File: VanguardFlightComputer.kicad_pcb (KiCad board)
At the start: 4 copper layers, 56 x 32 mm, 62 parts, among them IC1 ST1L05CPU33R, IC2 ASM330LHHTR, IC3 MAX-M10S-00B, J1 USB_C_Receptacle, J2 MEM2067-02-180-00-A, J3 Conn_Coaxial, J4 Conn_Coaxial, U1 STM32H743VGTx, U2 LD1117S50TR_SOT223, U3 USBLC6-2P6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

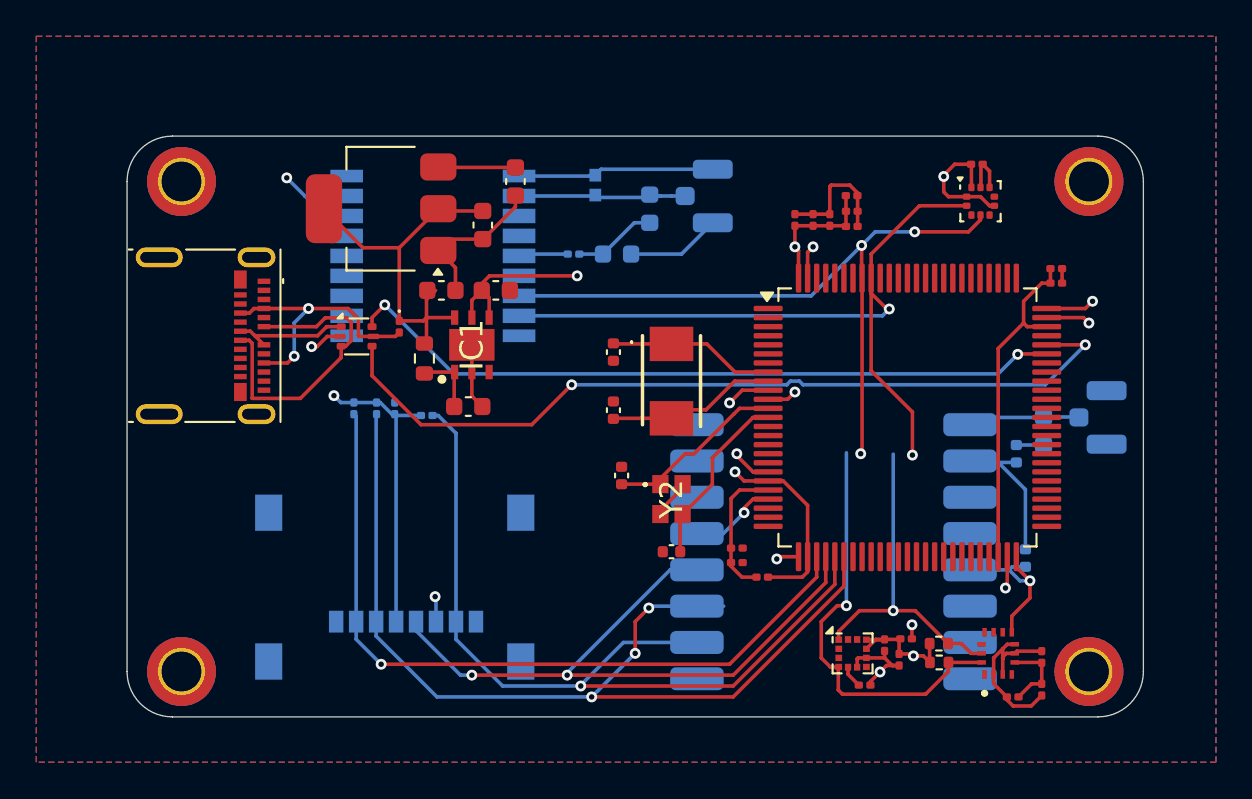
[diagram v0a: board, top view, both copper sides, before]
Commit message: Added IO
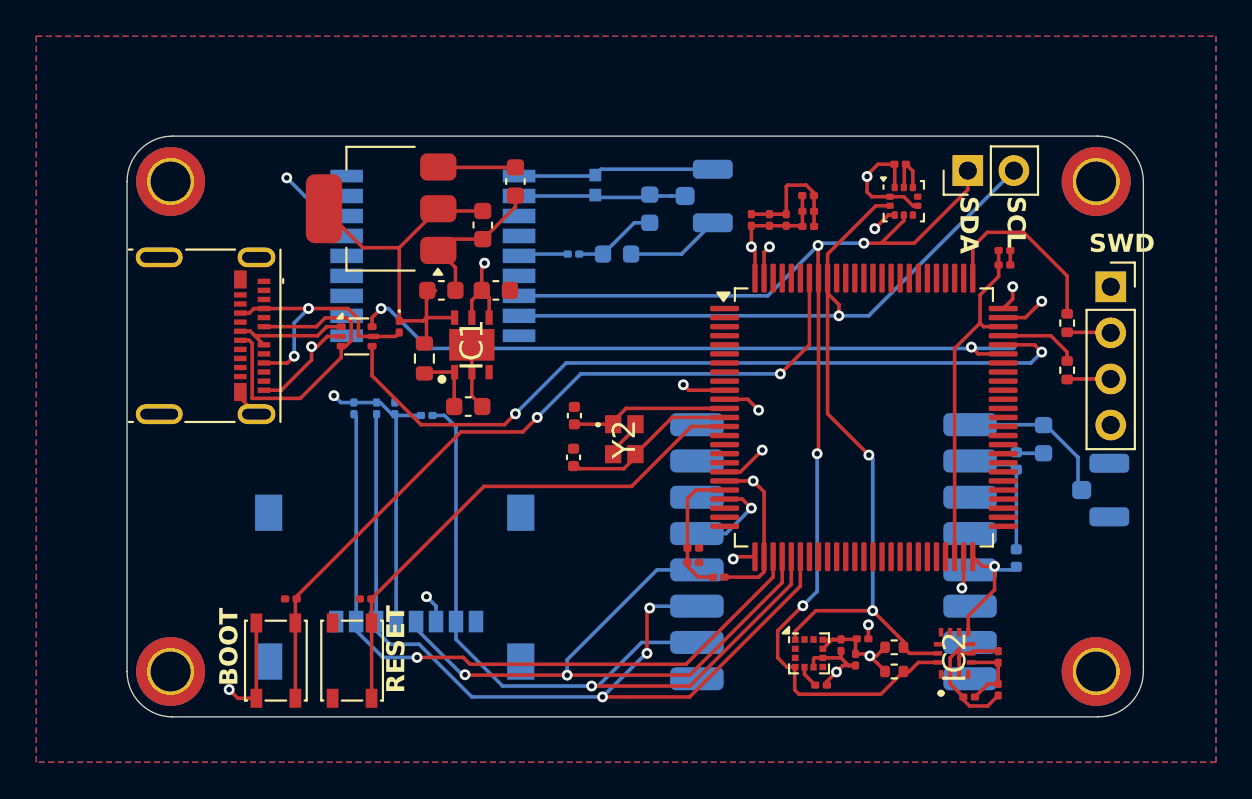
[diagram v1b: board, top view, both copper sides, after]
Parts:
- removed C16, C17: 10pF, Capacitor_SMD:C_0402_1005Metric
- removed Y1: 32.768MHz, VanguardLib:ABM3
- added C30: 100nF, Capacitor_SMD:C_0201_0603Metric, F.Cu at (103.1, 101.0)
- added J5: Conn_01x04_Pin, Connector_PinSocket_2.54mm:PinSocket_1x04_P2.54mm_Vertical, F.Cu at (144.2, 83.8)
- added J6: Conn_01x02_Pin, Connector_PinHeader_2.54mm:PinHeader_1x02_P2.54mm_Vertical, F.Cu at (136.3, 77.4)
- added R10: 100, Resistor_SMD:R_0402_1005Metric, F.Cu at (141.8, 85.8)
- added R8: 10k, Resistor_SMD:R_0201_0603Metric, F.Cu at (99.0, 101.0)
- added R9: 100, Resistor_SMD:R_0402_1005Metric, F.Cu at (141.8, 88.4)
- added SW1: SW_Push, Button_Switch_SMD:SW_SPST_PTS810, F.Cu at (102.4, 104.4)
- added SW2: SW_Push, Button_Switch_SMD:SW_SPST_PTS810, F.Cu at (98.2, 104.4)
- moved C19 7.50 mm to (114.6, 93.2), turned to -90 degrees
- moved C27 4.22 mm to (132.6, 77.0)
- moved U5 4.22 mm to (132.8, 79.1)
- moved C18 4.20 mm to (114.7, 90.9)
- moved Y2 4.20 mm to (117.4, 92.2)
- moved J4 4.00 mm to (143.7, 95.0)
- moved C14 3.03 mm to (138.3, 81.8)
- moved C15 3.03 mm to (138.3, 82.6)
- moved R3 2.90 mm to (132.3, 105.0)
- moved R2 2.61 mm to (132.3, 103.7)
- moved C5 2.40 mm to (126.3, 80.1)
- moved C20 2.40 mm to (138.0, 104.2)
- moved C21 2.40 mm to (138.0, 106.0)
- moved C22 2.40 mm to (136.4, 106.4)
- moved C24 2.40 mm to (130.5, 103.2)
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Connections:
- R2 pad 2: I2C1_SDA -> I2C1_SCL
- R3 pad 2: I2C1_SCL -> I2C1_SDA
- U1 pad 14: unconnected-(U1-NRST-Pad14) -> RST
- U1 pad 94: unconnected-(U1-BOOT0-Pad94) -> BOOT0
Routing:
- net BOOT0: track 0.00 -> 43.3 mm, vias 0 -> 2
- net RST: track 0.00 -> 28.9 mm
- net SWCLK: track 0.00 -> 10.3 mm
- net OSC32_OUT: track 9.59 -> 0.00 mm
- net OSC32_IN: track 9.38 -> 0.00 mm
- net I2C1_SCL: track 59.5 -> 68.1 mm
- net GND: track 82.1 -> 87.8 mm, vias 10 -> 11
- net SWDIO: track 0.00 -> 4.39 mm
- net SPI1_MOSI: track 53.9 -> 49.7 mm
- net SPI1_MISO: track 46.3 -> 43.4 mm
- net SD_CS: track 41.5 -> 38.8 mm
- net USB_DP: track 46.2 -> 43.6 mm
- net I2C1_SDA: track 62.6 -> 65.1 mm
- net Net-(J5-Pin_3): track 0.00 -> 2.41 mm
- net Net-(J5-Pin_2): track 0.00 -> 2.41 mm
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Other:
- board text added: "BOOT"
- board text added: "RESET"
- board text added: "SCL"
- board text added: "SDA"
- board text added: "SWD"

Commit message: Change 0201 to 0403
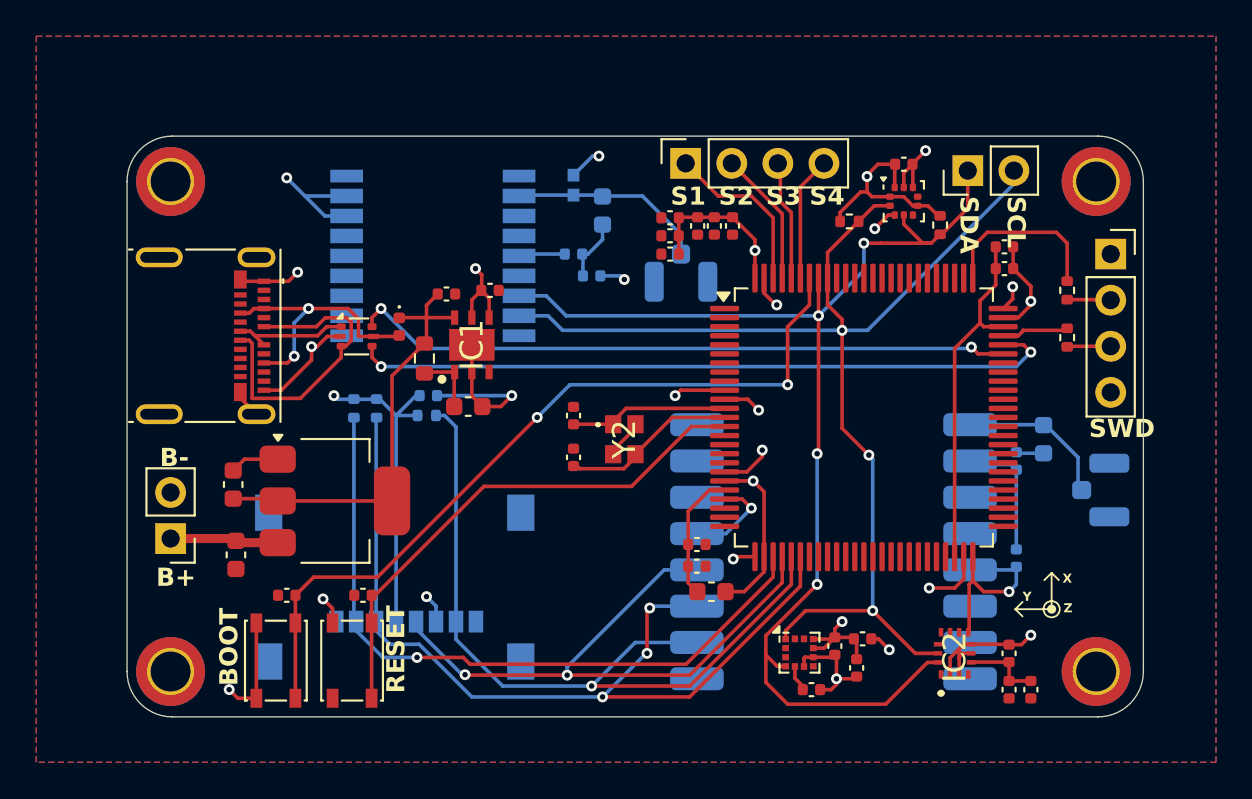
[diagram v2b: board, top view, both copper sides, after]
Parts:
- added J7: Conn_01x04_Pin, Connector_PinSocket_2.54mm:PinSocket_1x04_P2.54mm_Vertical, F.Cu at (120.8, 77.0)
- added J8: Conn_01x02_Pin, Connector_PinHeader_2.54mm:PinHeader_1x02_P2.54mm_Vertical, F.Cu at (92.4, 97.7)
- C1, C14, C15, C2, C20, C21, C22, C23, C24, C25, C26, C27, C28, C3, C30, C4, C5, C6, C7, C8: footprint Capacitor_SMD:C_0201_0603Metric -> Capacitor_SMD:C_0402_1005Metric
- C11, C12, C29: footprint Capacitor_SMD:C_0603_1608Metric -> Capacitor_SMD:C_0402_1005Metric
- D1: footprint Diode_SMD:D_0201_0603Metric -> Diode_SMD:D_0402_1005Metric
- FB1: footprint Capacitor_SMD:C_0201_0603Metric -> Capacitor_SMD:C_0603_1608Metric
- R4, R5, R6: footprint Resistor_SMD:R_0201_0603Metric -> Resistor_SMD:R_0402_1005Metric
- R7, R8: footprint Resistor_SMD:R_0201_0603Metric -> Capacitor_SMD:C_0402_1005Metric
- moved C9 25.7 mm to (96.0, 98.6)
- moved R3 24.7 mm to (134.8, 80.4), turned to -90 degrees
- moved R2 23.6 mm to (129.8, 80.2)
- moved C10 19.8 mm to (95.8, 94.7), turned to 90 degrees
- moved U2 16.3 mm to (101.5, 95.6), turned to 0 degrees
- moved C7 8.26 mm to (119.9, 82.0), turned to 180 degrees
- moved C6 7.73 mm to (119.9, 81.0), turned to 180 degrees
- moved C8 7.63 mm to (119.9, 80.0), turned to 180 degrees
- moved C5 4.90 mm to (121.4, 80.4), turned to -90 degrees
- moved J3 4.44 mm to (120.5, 83.0), turned to -90 degrees
- moved C22 3.42 mm to (139.8, 106.0), turned to -90 degrees
- moved C4 3.06 mm to (122.4, 80.4), turned to -90 degrees
- moved FB2 2.60 mm to (116.2, 79.6)
- moved C28 1.98 mm to (106.6, 89.8), turned to 0 degrees
- moved C29 1.84 mm to (115.6, 83.2)
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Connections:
- U1 pad 6: unconnected-(U1-VBAT-Pad6) -> +3.3V
- U1 pad 95: unconnected-(U1-PB8-Pad95) -> SERVO_4_PWM
- U1 pad 96: unconnected-(U1-PB9-Pad96) -> SERVO_3_PWM
- U1 pad 97: unconnected-(U1-PE0-Pad97) -> SERVO_2_PWM
- U1 pad 98: unconnected-(U1-PE1-Pad98) -> SERVO_1_PWM
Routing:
- net GND: track 87.8 -> 78.0 mm, vias 11 -> 18
- net SERVO_1_PWM: track 0.00 -> 9.39 mm
- net +3.3V: track 76.4 -> 85.2 mm
- net SERVO_2_PWM: track 0.00 -> 7.48 mm
- net SERVO_4_PWM: track 0.00 -> 6.86 mm
- net SERVO_3_PWM: track 0.00 -> 6.63 mm
- net USB_DP: track 43.6 -> 39.2 mm
- net I2C1_SDA: track 65.1 -> 69.3 mm
- net +5V: track 20.9 -> 24.3 mm
- net USB_DM: track 39.0 -> 36.6 mm
- net VIN: track 4.26 -> 6.03 mm
- net Net-(IC3-RF_IN): track 9.26 -> 10.9 mm
- net Net-(C29-Pad1): track 4.69 -> 3.80 mm
- net I2C1_SCL: track 68.1 -> 67.2 mm
- net SWCLK: track 10.3 -> 9.59 mm
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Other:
- board text added: "3.3V"
- board text added: "B+"
- board text added: "B-"
- board text added: "CLK"
- board text added: "DIO"
- board text added: "GND"
- board text added: "S1"
- board text added: "S2"
- board text added: "S3"
- board text added: "S4"
- board text added: "X"
- board text added: "Y"
- board text added: "Z"

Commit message: Re-Routed PCB
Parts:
- R8: footprint Capacitor_SMD:C_0402_1005Metric -> Resistor_SMD:R_0402_1005Metric
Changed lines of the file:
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@@
 		)
 	)
-	(footprint "Capacitor_SMD:C_0402_1005Metric"
+	(footprint "Resistor_SMD:R_0402_1005Metric"
 		(layer "F.Cu")
 		(at 98.8 100.8 180)
-		(descr "Capacitor SMD 0402 (1005 Metric), square (rectangular) end terminal, IPC_7351 nominal, (Body size source: IPC-SM-782 page 76, https://www.pcb-3d.com/wordpress/wp-content/uploads/ipc-sm-782a_amendment_1_and_2.pdf), generated with kicad-footprint-generator")
-		(tags "capacitor")
+		(descr "Resistor SMD 0402 (1005 Metric), square (rectangular) end terminal, IPC_7351 nominal, (Body size source: IPC-SM-782 page 72, https://www.pcb-3d.com/wordpress/wp-content/uploads/ipc-sm-782a_amendment_1_and_2.pdf), generated with kicad-footprint-generator")
+		(tags "resistor")
 		(property "Reference" "R8"
-			(at 0 -1.16 180)
+			(at 0 -1.17 180)
 			(layer "F.SilkS")
 			(hide yes)
@@
 		)
 		(property "Value" "10k"
-			(at 0 1.16 180)
+			(at 0 1.17 180)
 			(layer "F.Fab")
 			(hide yes)
@@
 			)
 		)
-		(property "Footprint" "Capacitor_SMD:C_0402_1005Metric"
+		(property "Footprint" "Resistor_SMD:R_0402_1005Metric"
 			(at 0 0 180)
 			(unlocked yes)
@@
 		(attr smd)
 		(fp_line
-			(start -0.107836 0.36)
-			(end 0.107836 0.36)
+			(start -0.153641 0.38)
+			(end 0.153641 0.38)
 			(stroke
 				(width 0.12)
@@
 		)
 		(fp_line
-			(start -0.107836 -0.36)
-			(end 0.107836 -0.36)
+			(start -0.153641 -0.38)
+			(end 0.153641 -0.38)
 			(stroke
 				(width 0.12)
@@
 		)
 		(fp_line
-			(start 0.91 0.46)
-			(end -0.91 0.46)
+			(start 0.93 0.47)
+			(end -0.93 0.47)
 			(stroke
 				(width 0.05)
@@
 		)
 		(fp_line
-			(start 0.91 -0.46)
-			(end 0.91 0.46)
+			(start 0.93 -0.47)
+			(end 0.93 0.47)
 			(stroke
 				(width 0.05)
@@
 		)
 		(fp_line
-			(start -0.91 0.46)
-			(end -0.91 -0.46)
+			(start -0.93 0.47)
+			(end -0.93 -0.47)
 			(stroke
 				(width 0.05)
@@
 		)
 		(fp_line
-			(start -0.91 -0.46)
-			(end 0.91 -0.46)
+			(start -0.93 -0.47)
+			(end 0.93 -0.47)
 			(stroke
 				(width 0.05)
@@
 		)
 		(fp_line
-			(start 0.5 0.25)
-			(end -0.5 0.25)
+			(start 0.525 0.27)
+			(end -0.525 0.27)
 			(stroke
 				(width 0.1)
@@
 		)
 		(fp_line
-			(start 0.5 -0.25)
-			(end 0.5 0.25)
+			(start 0.525 -0.27)
+			(end 0.525 0.27)
 			(stroke
 				(width 0.1)
@@
 		)
 		(fp_line
-			(start -0.5 0.25)
-			(end -0.5 -0.25)
+			(start -0.525 0.27)
+			(end -0.525 -0.27)
 			(stroke
 				(width 0.1)
@@
 		)
 		(fp_line
-			(start -0.5 -0.25)
-			(end 0.5 -0.25)
+			(start -0.525 -0.27)
+			(end 0.525 -0.27)
 			(stroke
 				(width 0.1)
@@
 			(effects
 				(font
-					(size 0.25 0.25)
+					(size 0.26 0.26)
 					(thickness 0.04)
 				)
@@
 		)
 		(pad "1" smd roundrect
-			(at -0.48 0 180)
-			(size 0.56 0.62)
+			(at -0.51 0 180)
+			(size 0.54 0.64)
 			(layers "F.Cu" "F.Paste" "F.Mask")
 			(roundrect_rratio 0.25)
@@
 		)
 		(pad "2" smd roundrect
-			(at 0.48 0 180)
-			(size 0.56 0.62)
+			(at 0.51 0 180)
+			(size 0.54 0.64)
 			(layers "F.Cu" "F.Paste" "F.Mask")
 			(roundrect_rratio 0.25)
@@
 			(pintype "passive")
 		)
-		(model "${KICAD8_3DMODEL_DIR}/Capacitor_SMD.3dshapes/C_0402_1005Metric.wrl"
+		(model "${KICAD8_3DMODEL_DIR}/Resistor_SMD.3dshapes/R_0402_1005Metric.wrl"
 			(offset
 				(xyz 0 0 0)
@@
 		(sheetname "IO")
 		(sheetfile "io.kicad_sch")
+		(zone_connect 0)
 		(attr smd)
 		(fp_line
@@
 		(tags "capacitor")
 		(property "Reference" "C28"
-			(at 0 1.16 360)
+			(at 0 1.16 0)
 			(layer "B.SilkS")
 			(hide yes)
@@
 		)
 		(property "Value" "100nF"
-			(at 0 -1.16 360)
+			(at 0 -1.16 0)
 			(layer "B.Fab")
 			(hide yes)
@@
 		)
 		(fp_text user "${REFERENCE}"
-			(at 0 0 360)
+			(at 0 0 0)
 			(layer "B.Fab")
 			(effects
